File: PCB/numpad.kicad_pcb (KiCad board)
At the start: 2 copper layers, 106.4 x 115.1 mm, 72 parts, among them J1 AVR-ISP-6, J2 Conn_01x04_Female, SW1 SW_Push, U1 ProMicro

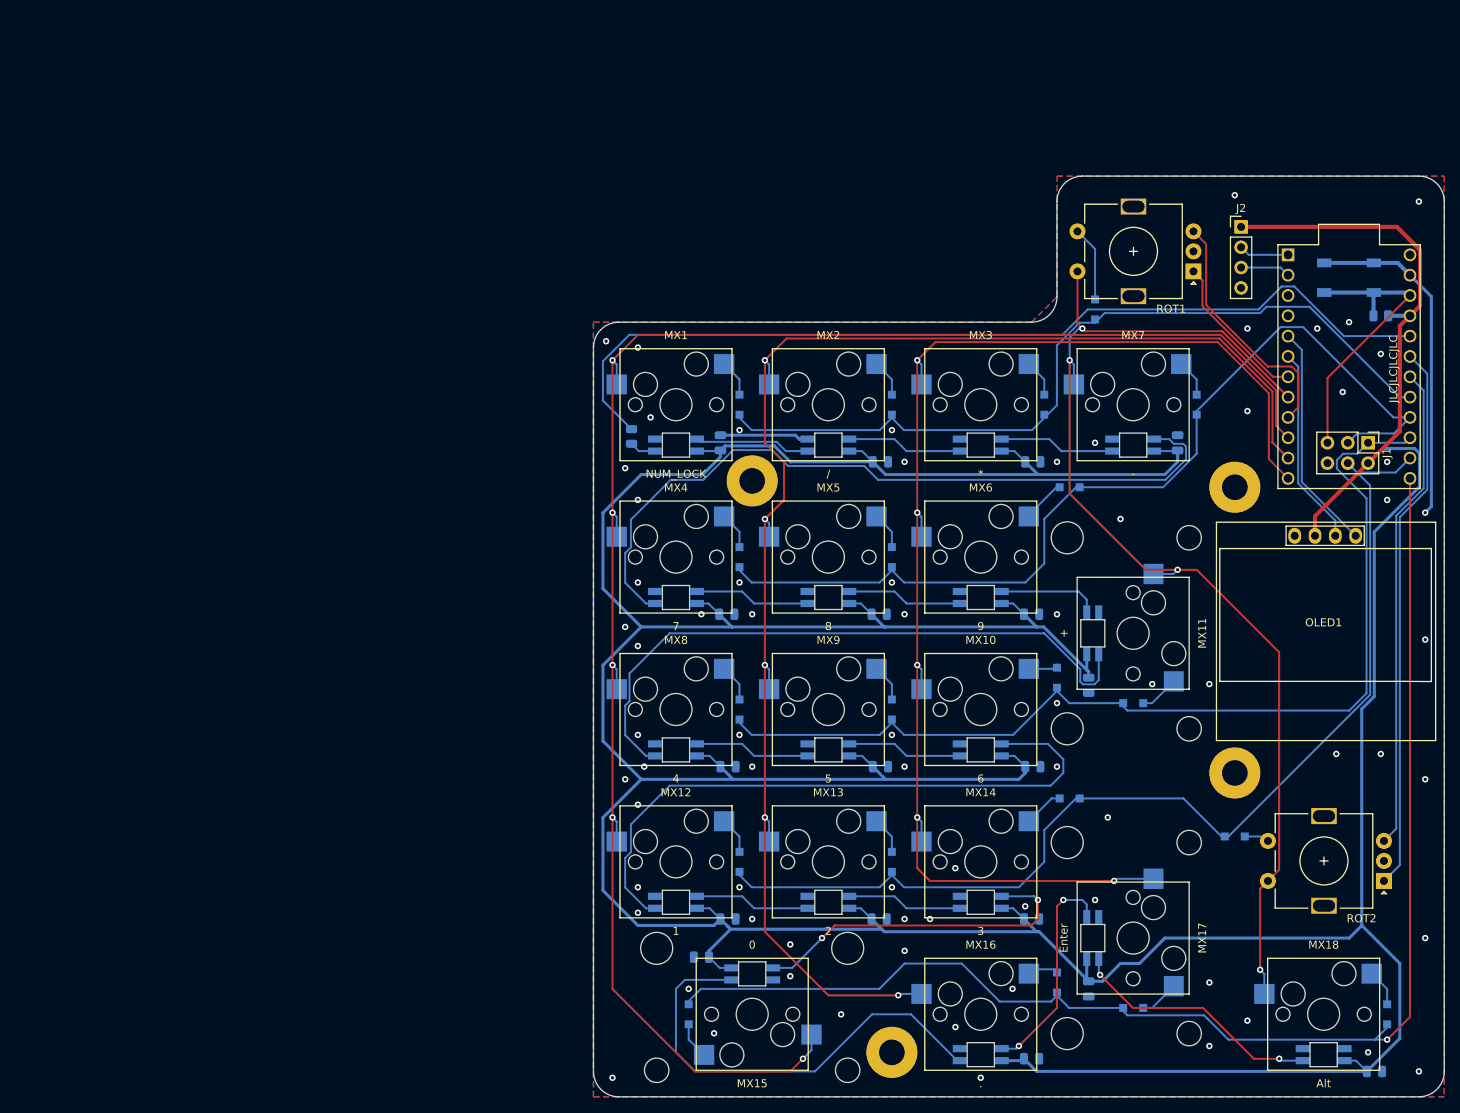
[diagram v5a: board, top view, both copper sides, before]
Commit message: Updated to kicad 6
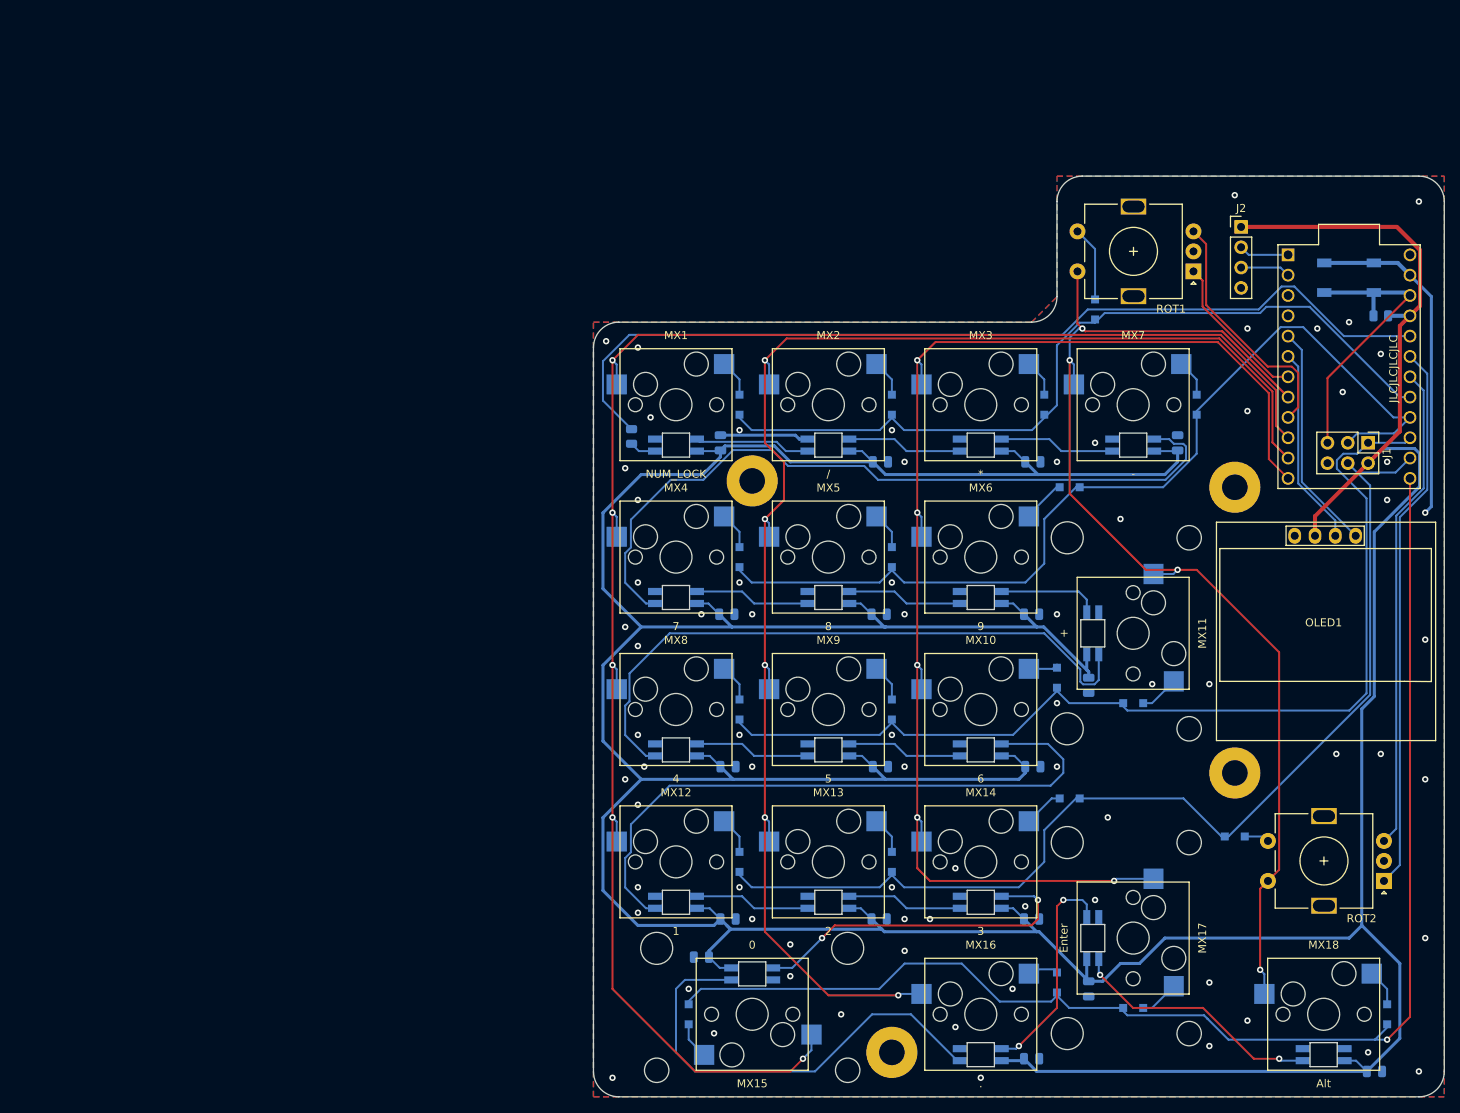
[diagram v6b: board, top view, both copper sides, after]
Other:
- net class Default removed

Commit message: Completely redid schematic and PCB
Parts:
- removed LC1, LC10, LC11, LC12, LC13, LC14, LC15, LC16, LC17, LC18, LC2, LC3, LC4, LC5, LC6, LC7, LC8, LC9: 10uF, Capacitor_SMD:C_0805_2012Metric
- added C1: 100nF, Capacitor_SMD:C_0603_1608Metric, B.Cu at (92.9, 96.8)
- added C10: 100nF, Capacitor_SMD:C_0603_1608Metric, B.Cu at (113.5, 132.6)
- added C11: 100nF, Capacitor_SMD:C_0603_1608Metric, B.Cu at (132.6, 132.6)
- added C12: 100nF, Capacitor_SMD:C_0603_1608Metric, B.Cu at (94.5, 151.6)
- added C13: 100nF, Capacitor_SMD:C_0603_1608Metric, B.Cu at (113.5, 151.6)
- added C14: 100nF, Capacitor_SMD:C_0603_1608Metric, B.Cu at (132.6, 151.6)
- added C15: 100nF, Capacitor_SMD:C_0603_1608Metric, B.Cu at (140.5, 161.1)
- added C16: 100nF, Capacitor_SMD:C_0603_1608Metric, B.Cu at (104.0, 170.7)
- added C17: 100nF, Capacitor_SMD:C_0603_1608Metric, B.Cu at (132.6, 170.7)
- added C18: 100nF, Capacitor_SMD:C_0603_1608Metric, B.Cu at (175.4, 170.7)
- added C2: 100nF, Capacitor_SMD:C_0603_1608Metric, B.Cu at (113.5, 94.5)
- added C3: 100nF, Capacitor_SMD:C_0603_1608Metric, B.Cu at (132.6, 94.5)
- added C4: 100nF, Capacitor_SMD:C_0603_1608Metric, B.Cu at (151.6, 94.5)
- added C5: 100nF, Capacitor_SMD:C_0603_1608Metric, B.Cu at (94.5, 113.5)
- added C6: 100nF, Capacitor_SMD:C_0603_1608Metric, B.Cu at (113.5, 113.5)
- added C7: 100nF, Capacitor_SMD:C_0603_1608Metric, B.Cu at (132.6, 113.5)
- added C8: 100nF, Capacitor_SMD:C_0603_1608Metric, B.Cu at (140.5, 123.0)
- added C9: 100nF, Capacitor_SMD:C_0603_1608Metric, B.Cu at (94.5, 132.6)
- added LED1: SK6812MINI-E, custom_footprints:YS-SK6812MINI-E, B.Cu at (88.9, 93.7)
- added LED10: SK6812MINI-E, custom_footprints:YS-SK6812MINI-E, B.Cu at (107.9, 131.8)
- added LED11: SK6812MINI-E, custom_footprints:YS-SK6812MINI-E, B.Cu at (127.0, 131.8)
- added LED12: SK6812MINI-E, custom_footprints:YS-SK6812MINI-E, B.Cu at (88.9, 150.8)
- added LED13: SK6812MINI-E, custom_footprints:YS-SK6812MINI-E, B.Cu at (107.9, 150.8)
- added LED14: SK6812MINI-E, custom_footprints:YS-SK6812MINI-E, B.Cu at (127.0, 150.8)
- added LED15: SK6812MINI-E, custom_footprints:YS-SK6812MINI-E, B.Cu at (141.3, 155.6)
- added LED16: SK6812MINI-E, custom_footprints:YS-SK6812MINI-E, B.Cu at (98.4, 169.9)
- added LED17: SK6812MINI-E, custom_footprints:YS-SK6812MINI-E, B.Cu at (127.0, 169.9)
- added LED18: SK6812MINI-E, custom_footprints:YS-SK6812MINI-E, B.Cu at (169.9, 169.9)
- added LED2: SK6812MINI-E, custom_footprints:YS-SK6812MINI-E, B.Cu at (107.9, 93.7)
- added LED3: SK6812MINI-E, custom_footprints:YS-SK6812MINI-E, B.Cu at (127.0, 93.7)
- added LED4: SK6812MINI-E, custom_footprints:YS-SK6812MINI-E, B.Cu at (146.0, 93.7)
- added LED5: SK6812MINI-E, custom_footprints:YS-SK6812MINI-E, B.Cu at (88.9, 112.7)
- added LED6: SK6812MINI-E, custom_footprints:YS-SK6812MINI-E, B.Cu at (107.9, 112.7)
- added LED7: SK6812MINI-E, custom_footprints:YS-SK6812MINI-E, B.Cu at (127.0, 112.7)
- added LED8: SK6812MINI-E, custom_footprints:YS-SK6812MINI-E, B.Cu at (141.3, 117.5)
- added LED9: SK6812MINI-E, custom_footprints:YS-SK6812MINI-E, B.Cu at (88.9, 131.8)
- added R3: 470, Resistor_SMD:R_0603_1608Metric, B.Cu at (175.4, 169.1)
- D1, D10, D11, D12, D13, D14, D15, D16, D17, D18, D2, D3, D4, D5, D6, D7, D8, D9, RD1, RD2: value SOD-123 -> D_Small; footprint Diode_SMD:D_SOD-323_HandSoldering -> Diode_SMD:D_SOD-123
- MX1: value NUM_LOCK -> CherryMX; footprint CherryMX_PCB_KailhSocket_LTST-A683CEGBW:CherryMX_1.00u_PCB_KailhSocket_LTST-A683CEGBW -> CherryMX_PCB_KailhSocket:CherryMX_1.00u_PCB_KailhSocket
- MX10: value 6 -> CherryMX; footprint CherryMX_PCB_KailhSocket_LTST-A683CEGBW:CherryMX_1.00u_PCB_KailhSocket_LTST-A683CEGBW -> CherryMX_PCB_KailhSocket:CherryMX_1.00u_PCB_KailhSocket
- MX11: value + -> CherryMX; footprint CherryMX_PCB_KailhSocket_StabWireBottom_LTST-A683CEGBW:CherryMX_2.00u_PCB_KailhSocket_StabWireBottom_LTST-A683CEGBW -> CherryMX_PCB_KailhSocket_StabWireBottom:CherryMX_2.00u_PCB_KailhSocket_StabWireBottom
- MX12: value 1 -> CherryMX; footprint CherryMX_PCB_KailhSocket_LTST-A683CEGBW:CherryMX_1.00u_PCB_KailhSocket_LTST-A683CEGBW -> CherryMX_PCB_KailhSocket:CherryMX_1.00u_PCB_KailhSocket
- MX13: value 2 -> CherryMX; footprint CherryMX_PCB_KailhSocket_LTST-A683CEGBW:CherryMX_1.00u_PCB_KailhSocket_LTST-A683CEGBW -> CherryMX_PCB_KailhSocket:CherryMX_1.00u_PCB_KailhSocket
- MX14: value 3 -> CherryMX; footprint CherryMX_PCB_KailhSocket_LTST-A683CEGBW:CherryMX_1.00u_PCB_KailhSocket_LTST-A683CEGBW -> CherryMX_PCB_KailhSocket:CherryMX_1.00u_PCB_KailhSocket
- MX15: value 0 -> CherryMX; footprint CherryMX_PCB_KailhSocket_StabWireBottom_LTST-A683CEGBW:CherryMX_2.00u_PCB_KailhSocket_StabWireBottom_LTST-A683CEGBW -> CherryMX_PCB_KailhSocket_StabWireTop:CherryMX_2.00u_PCB_KailhSocket_StabWireTop
- MX16: value . -> CherryMX; footprint CherryMX_PCB_KailhSocket_LTST-A683CEGBW:CherryMX_1.00u_PCB_KailhSocket_LTST-A683CEGBW -> CherryMX_PCB_KailhSocket:CherryMX_1.00u_PCB_KailhSocket
- MX17: value Enter -> CherryMX; footprint CherryMX_PCB_KailhSocket_StabWireBottom_LTST-A683CEGBW:CherryMX_2.00u_PCB_KailhSocket_StabWireBottom_LTST-A683CEGBW -> CherryMX_PCB_KailhSocket_StabWireBottom:CherryMX_2.00u_PCB_KailhSocket_StabWireBottom
- MX18: value Alt -> CherryMX; footprint CherryMX_PCB_KailhSocket_LTST-A683CEGBW:CherryMX_1.50u_PCB_KailhSocket_LTST-A683CEGBW -> CherryMX_PCB_KailhSocket:CherryMX_1.50u_PCB_KailhSocket
- MX2: value / -> CherryMX; footprint CherryMX_PCB_KailhSocket_LTST-A683CEGBW:CherryMX_1.00u_PCB_KailhSocket_LTST-A683CEGBW -> CherryMX_PCB_KailhSocket:CherryMX_1.00u_PCB_KailhSocket
- MX3: value * -> CherryMX; footprint CherryMX_PCB_KailhSocket_LTST-A683CEGBW:CherryMX_1.00u_PCB_KailhSocket_LTST-A683CEGBW -> CherryMX_PCB_KailhSocket:CherryMX_1.00u_PCB_KailhSocket
- MX4: value 7 -> CherryMX; footprint CherryMX_PCB_KailhSocket_LTST-A683CEGBW:CherryMX_1.00u_PCB_KailhSocket_LTST-A683CEGBW -> CherryMX_PCB_KailhSocket:CherryMX_1.00u_PCB_KailhSocket
- MX5: value 8 -> CherryMX; footprint CherryMX_PCB_KailhSocket_LTST-A683CEGBW:CherryMX_1.00u_PCB_KailhSocket_LTST-A683CEGBW -> CherryMX_PCB_KailhSocket:CherryMX_1.00u_PCB_KailhSocket
- MX6: value 9 -> CherryMX; footprint CherryMX_PCB_KailhSocket_LTST-A683CEGBW:CherryMX_1.00u_PCB_KailhSocket_LTST-A683CEGBW -> CherryMX_PCB_KailhSocket:CherryMX_1.00u_PCB_KailhSocket
- MX7: value - -> CherryMX; footprint CherryMX_PCB_KailhSocket_LTST-A683CEGBW:CherryMX_1.00u_PCB_KailhSocket_LTST-A683CEGBW -> CherryMX_PCB_KailhSocket:CherryMX_1.00u_PCB_KailhSocket
- MX8: value 4 -> CherryMX; footprint CherryMX_PCB_KailhSocket_LTST-A683CEGBW:CherryMX_1.00u_PCB_KailhSocket_LTST-A683CEGBW -> CherryMX_PCB_KailhSocket:CherryMX_1.00u_PCB_KailhSocket
- MX9: value 5 -> CherryMX; footprint CherryMX_PCB_KailhSocket_LTST-A683CEGBW:CherryMX_1.00u_PCB_KailhSocket_LTST-A683CEGBW -> CherryMX_PCB_KailhSocket:CherryMX_1.00u_PCB_KailhSocket
- R1, R2: footprint Resistor_SMD:R_0805_2012Metric -> Resistor_SMD:R_0603_1608Metric
- moved H3 60.3 mm to (98.4, 98.4)
- moved H4 47.7 mm to (146.1, 100.8)
- moved D15 15.9 mm to (106.4, 165.1), turned to 90 degrees
- moved H2 12.8 mm to (146.0, 136.5)
- moved RD2 11.6 mm to (169.9, 146.0), turned to 90 degrees
- moved D6 10.8 mm to (134.9, 109.5), turned to 90 degrees
- moved D14 10.0 mm to (134.9, 147.6), turned to 90 degrees
- moved D17 3.98 mm to (148.4, 167.5), turned to 90 degrees
- moved D11 3.97 mm to (148.4, 129.4), turned to 90 degrees
- moved RD1 3.96 mm to (138.1, 79.4)
- moved R2 3.54 mm to (173.8, 76.2)
- moved J1 3.54 mm to (172.2, 92.1)
- moved SW1 3.54 mm to (169.9, 71.4)
- moved U1 3.54 mm to (169.9, 82.5)
- moved R1 1.59 mm to (83.3, 94.5), turned to 0 degrees
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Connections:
- R1 pad 1: Net-(MX1-Pad4) -> BKL_DATA_IN
- R1 pad 2: BKL_DATA_IN -> Net-(LED1-Pad4)
- U1 pad 24: (no net) -> unconnected-(U1-Pad24)
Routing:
- net Net-(LED4-Pad2): track 0.00 -> 105.9 mm
- net DOUT1: track 94.6 -> 0.00 mm
- net Net-(LED8-Pad2): track 0.00 -> 84.9 mm, vias 0 -> 2
- net Net-(LED11-Pad2): track 0.00 -> 84.3 mm
- net DOUT3: track 80.5 -> 0.00 mm
- net DOUT4: track 80.0 -> 0.00 mm
- net Net-(LED15-Pad2): track 0.00 -> 76.4 mm, vias 0 -> 2
- net Net-(MX15-Pad5): track 57.2 -> 0.00 mm
- net DOUT5: track 42.8 -> 0.00 mm, vias 2 -> 0
- net Net-(LED17-Pad2): track 0.00 -> 37.9 mm
- net Net-(MX17-Pad5): track 31.9 -> 0.00 mm, vias 2 -> 0
- net COL0: track 217.4 -> 188.7 mm
- net Net-(MX16-Pad5): track 27.6 -> 0.00 mm, vias 2 -> 0
- net Net-(LED16-Pad2): track 0.00 -> 24.9 mm
- net GND: track 53.6 -> 69.9 mm, vias 74 -> 69
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- added copper zone on B.Cu, net ROW1

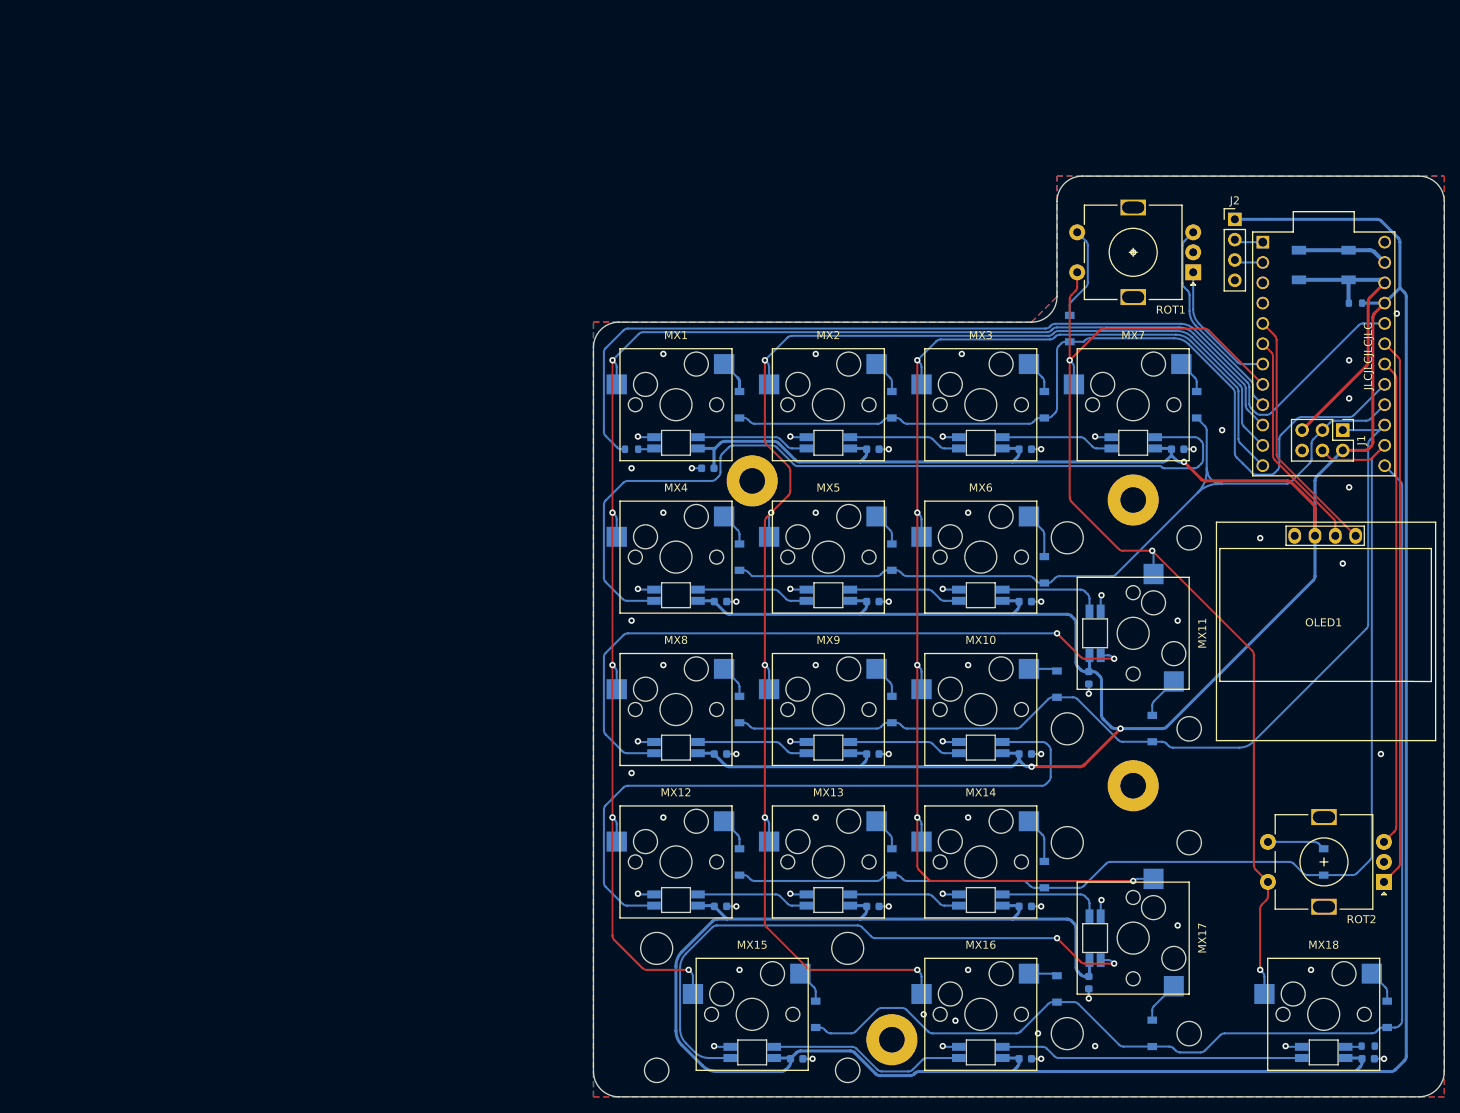
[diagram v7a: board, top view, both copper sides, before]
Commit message: Cleanup and exported gerbers
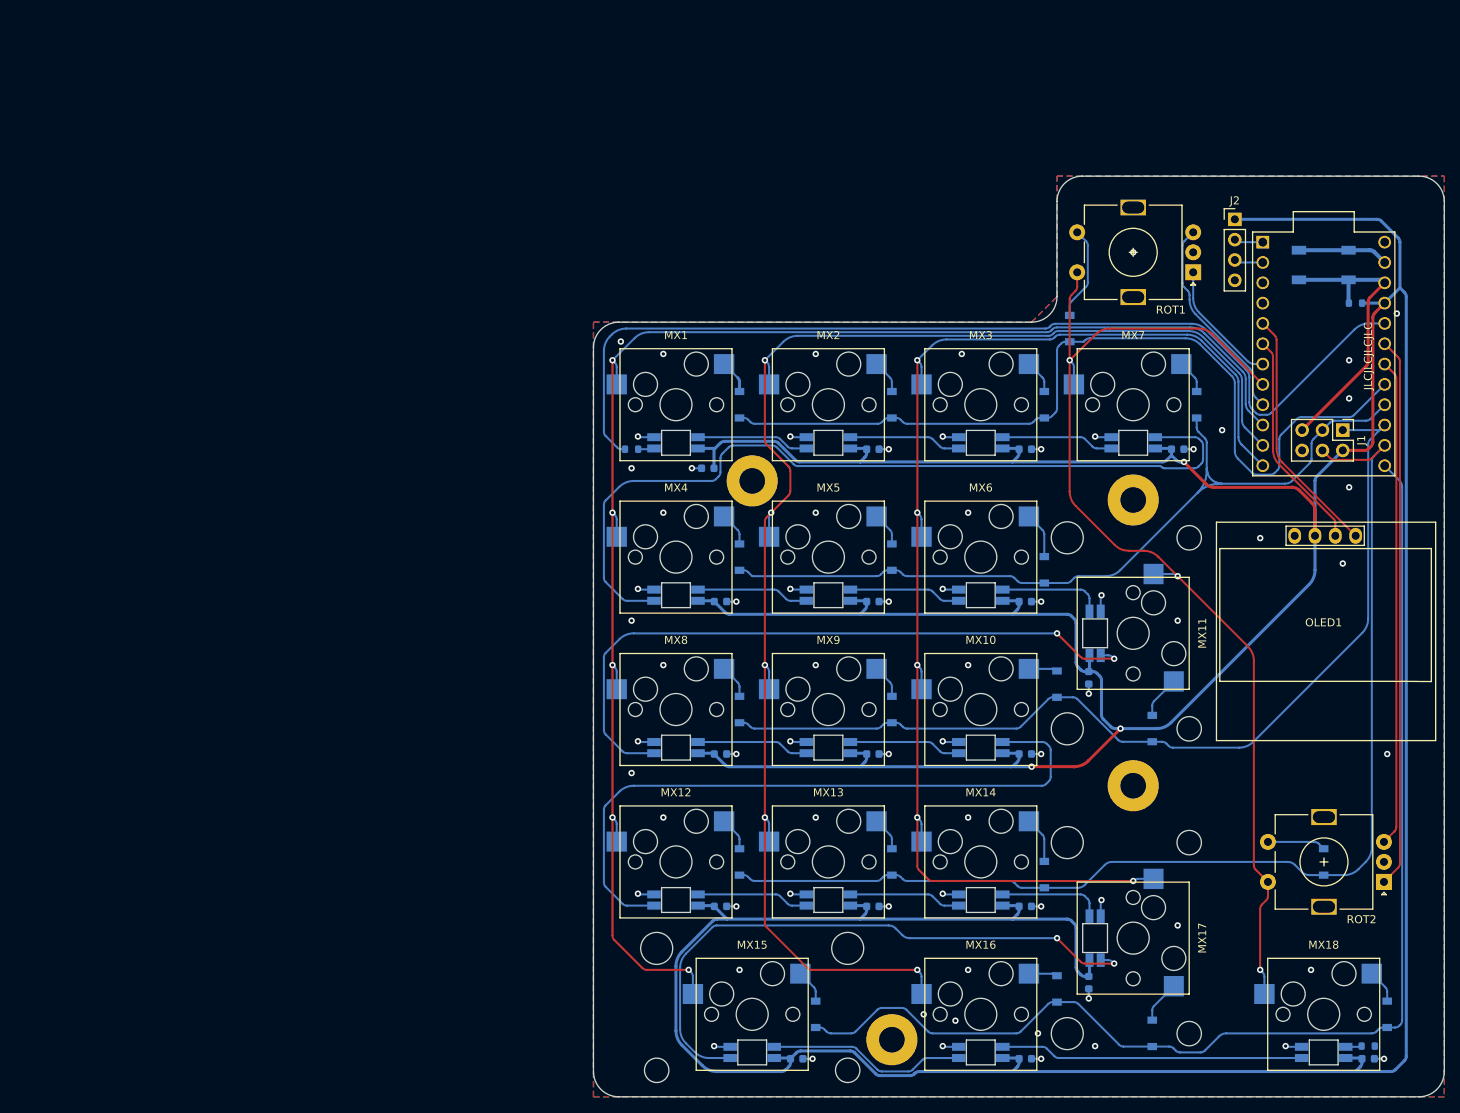
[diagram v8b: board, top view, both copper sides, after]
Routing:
- net BKL_DATA_IN: track 123.4 -> 124.5 mm
- net ENC_A1: track 16.6 -> 15.8 mm
- net ROW0: track 107.7 -> 108.5 mm
- net COL0: track 188.7 -> 189.4 mm
- net COL1: track 182.4 -> 183.1 mm
- net COL2: track 161.3 -> 162.0 mm
- net ROW1: track 104.1 -> 104.8 mm
- net GND: vias 69 -> 70
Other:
- board text added: "kb.ht12345.xyz/np0"
- board text removed: "kb.ht12345.xyz/numpad"
